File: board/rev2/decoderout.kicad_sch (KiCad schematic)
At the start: 12 parts, among them U10 IS61LV256AL, U11 74AHCT595

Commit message: Board GPIO allocation
- and usbmux

still need to do termination on the big buses + a bunch of bypass caps
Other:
- company: (none) -> MLABS
- title: (none) -> LED Bitstream Generator (gamma LUT + shifter)
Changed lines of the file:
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@@
 	(generator_version "9.0")
 	(paper "A4")
+	(title_block
+		(title "LED Bitstream Generator (gamma LUT + shifter)")
+		(rev "A")
+		(company "MLABS")
+		(comment 1 "MSign-NG")
+	)
 	(text "Gamma correction table (PIX_MEM)"
 		(exclude_from_sim no)

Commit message: Continue board, assign caps/res, adjust for JLC availability
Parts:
- C31, C32: footprint (none) -> Capacitor_SMD:C_0402_1005Metric; Part (none) -> CL05B104KB54PNC
- R13, R14, R15, R16, R17, R18, R19: footprint (none) -> Resistor_SMD:R_0402_1005Metric; Part (none) -> 0402WGF1001TCE
- R20: footprint (none) -> Resistor_SMD:R_0805_2012Metric; Part (none) -> 0805W8F1002T5E
- U11: footprint (none) -> Package_SO:TSSOP-16_4.4x5mm_P0.65mm
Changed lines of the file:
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@@
 			)
 		)
-		(property "Footprint" ""
+		(property "Footprint" "Capacitor_SMD:C_0402_1005Metric"
 			(at 114.3 73.66 0)
 			(effects
@@
 			)
 		)
+		(property "Part" "CL05B104KB54PNC"
+			(at 114.3 73.66 90)
+			(effects
+				(font
+					(size 1.27 1.27)
+				)
+				(hide yes)
+			)
+		)
 		(pin "2"
 		)
@@
 			)
 		)
-		(property "Footprint" ""
+		(property "Footprint" "Resistor_SMD:R_0402_1005Metric"
 			(at 139.7 102.87 0)
 			(effects
@@
 			)
 		)
+		(property "Part" "0402WGF1001TCE"
+			(at 139.7 102.87 90)
+			(effects
+				(font
+					(size 1.27 1.27)
+				)
+				(hide yes)
+			)
+		)
 		(pin "2"
 		)
@@
 			)
 		)
-		(property "Footprint" ""
+		(property "Footprint" "Resistor_SMD:R_0402_1005Metric"
 			(at 139.7 95.25 0)
 			(effects
@@
 			)
 		)
+		(property "Part" "0402WGF1001TCE"
+			(at 139.7 95.25 90)
+			(effects
+				(font
+					(size 1.27 1.27)
+				)
+				(hide yes)
+			)
+		)
 		(pin "2"
 		)
@@
 			)
 		)
-		(property "Footprint" ""
+		(property "Footprint" "Resistor_SMD:R_0402_1005Metric"
 			(at 139.7 105.41 0)
 			(effects
@@
 					(size 1.27 1.27)
 					(color 255 255 194 1)
+				)
+				(hide yes)
+			)
+		)
+		(property "Part" "0402WGF1001TCE"
+			(at 139.7 105.41 90)
+			(effects
+				(font
+					(size 1.27 1.27)
 				)
 				(hide yes)
@@
 			)
 		)
-		(property "Footprint" ""
+		(property "Footprint" "Package_SO:TSSOP-16_4.4x5mm_P0.65mm"
 			(at 184.15 97.79 0)
 			(effects
@@
 			)
 		)
-		(property "Footprint" ""
+		(property "Footprint" "Resistor_SMD:R_0402_1005Metric"
 			(at 139.7 100.33 0)
 			(effects
@@
 			)
 		)
+		(property "Part" "0402WGF1001TCE"
+			(at 139.7 100.33 90)
+			(effects
+				(font
+					(size 1.27 1.27)
+				)
+				(hide yes)
+			)
+		)
 		(pin "2"
 		)
@@
 			)
 		)
-		(property "Footprint" ""
+		(property "Footprint" "Resistor_SMD:R_0402_1005Metric"
 			(at 139.7 92.71 0)
 			(effects
@@
 			)
 		)
+		(property "Part" "0402WGF1001TCE"
+			(at 139.7 92.71 90)
+			(effects
+				(font
+					(size 1.27 1.27)
+				)
+				(hide yes)
+			)
+		)
 		(pin "2"
 		)
@@
 			)
 		)
-		(property "Footprint" ""
+		(property "Footprint" "Resistor_SMD:R_0402_1005Metric"
 			(at 139.7 97.79 0)
 			(effects
@@
 					(size 1.27 1.27)
 					(color 255 255 194 1)
+				)
+				(hide yes)
+			)
+		)
+		(property "Part" "0402WGF1001TCE"
+			(at 139.7 97.79 90)
+			(effects
+				(font
+					(size 1.27 1.27)
 				)
 				(hide yes)
@@
 			)
 		)
-		(property "Footprint" ""
+		(property "Footprint" "Capacitor_SMD:C_0402_1005Metric"
 			(at 191.77 76.2 0)
 			(effects
@@
 			)
 		)
+		(property "Part" "CL05B104KB54PNC"
+			(at 191.77 76.2 90)
+			(effects
+				(font
+					(size 1.27 1.27)
+				)
+				(hide yes)
+			)
+		)
 		(pin "2"
 		)
@@
 			)
 		)
-		(property "Footprint" ""
+		(property "Footprint" "Resistor_SMD:R_0402_1005Metric"
 			(at 139.7 90.17 0)
 			(effects
@@
 					(size 1.27 1.27)
 					(color 255 255 194 1)
+				)
+				(hide yes)
+			)
+		)
+		(property "Part" "0402WGF1001TCE"
+			(at 139.7 90.17 90)
+			(effects
+				(font
+					(size 1.27 1.27)
 				)
 				(hide yes)
@@
 			)
 		)
-		(property "Footprint" ""
+		(property "Footprint" "Resistor_SMD:R_0805_2012Metric"
 			(at 165.1 83.82 0)
 			(effects
@@
 				)
 				(hide yes)
+			)
+		)
+		(property "Part" "0805W8F1002T5E"
+			(at 165.1 83.82 0)
+			(effects
+				(font
+					(size 1.27 1.27)
+				)
+				(hide yes)

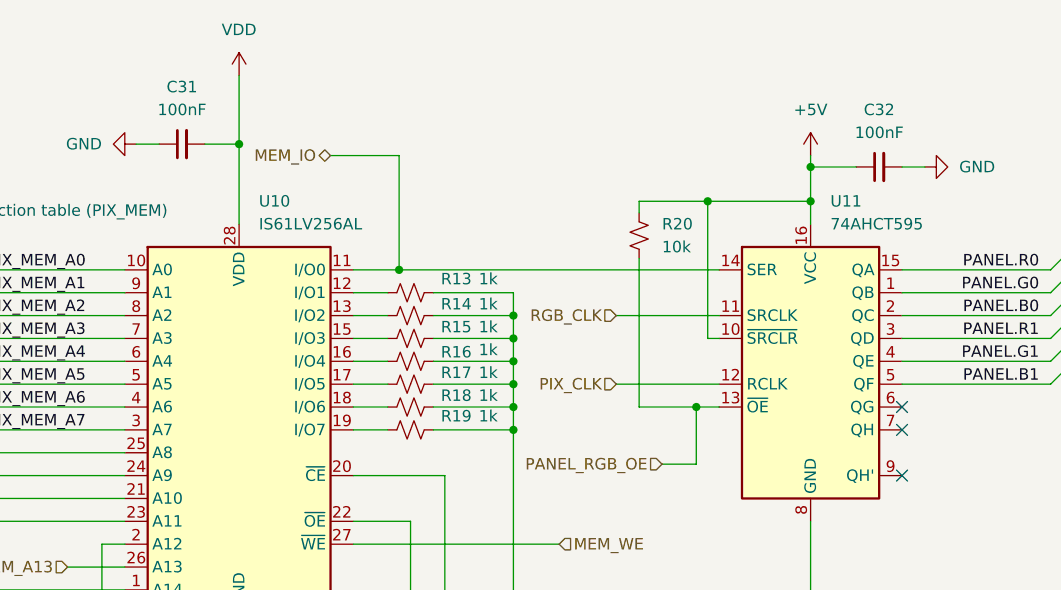
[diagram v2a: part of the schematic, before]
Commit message: Start new PCB
- all footprints setup
- need to setup netclasses next, tho
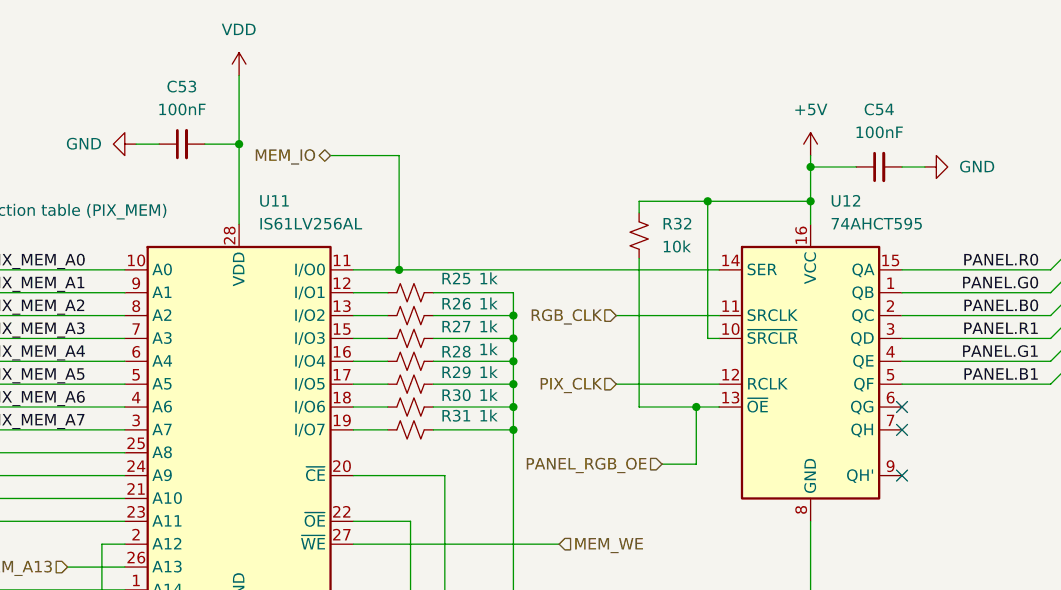
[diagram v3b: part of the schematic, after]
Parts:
- U11: renamed from U10; footprint Package_SO:SOP-28_8.4x18.16mm_P1.27mm -> Package_TSOPI:TSOP-28_L11.8-W8.0-P0.55-LS13.4-L; Part (none) -> IS61LV256AL
- U12: renamed from U11; Part (none) -> 74AHCT595
- renumbered C31 to C53, C32 to C54, R13 to R25, R14 to R26, R15 to R27, R16 to R28, R17 to R29, R18 to R30, R19 to R31, R20 to R32

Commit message: Really finish rev2 board schematic
- fix some more footprints
  - move to real SD card holder, for example
- repair part numbers
- add LCSC part refs to everything
- add even more caps to the 3.3V reg output
  - really should use an LDO but meh it should be fine

total BOM cost for 5 of them is apparently 160 CAD, or like 32 dollars
each (don't think that includes the feeder fees tho)
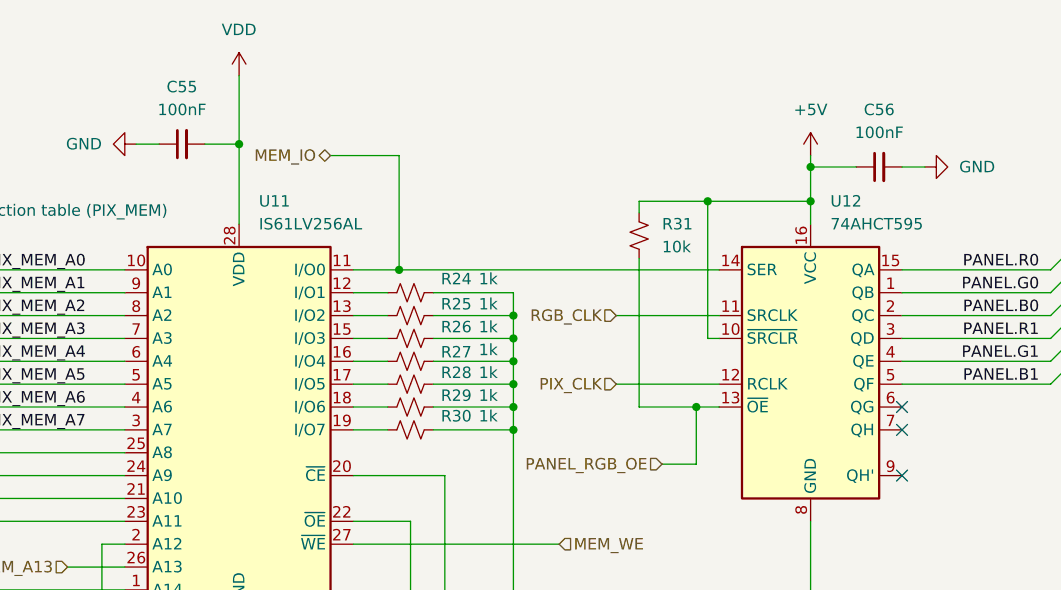
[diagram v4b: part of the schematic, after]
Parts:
- C55: renamed from C53; LCSC (none) -> C307331
- C56: renamed from C54; LCSC (none) -> C307331
- R24: renamed from R25; LCSC (none) -> C11702
- R25: renamed from R26; LCSC (none) -> C11702
- R26: renamed from R27; LCSC (none) -> C11702
- R27: renamed from R28; LCSC (none) -> C11702
- R28: renamed from R29; LCSC (none) -> C11702
- R29: renamed from R30; LCSC (none) -> C11702
- R30: renamed from R31; LCSC (none) -> C11702
- R31: renamed from R32; LCSC (none) -> C17414
- U11: LCSC (none) -> C412837; Part IS61LV256AL -> IS61LV256AL-10TLI
- U12: LCSC (none) -> C460504; Part 74AHCT595 -> 74AHCT595T16-13

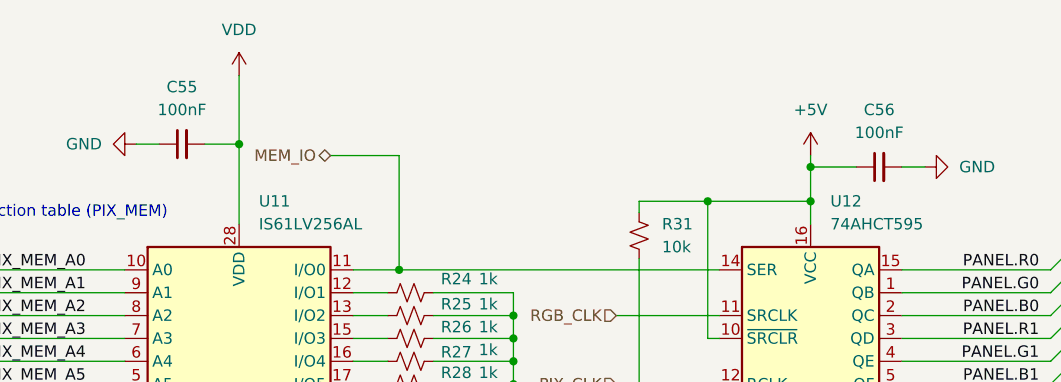
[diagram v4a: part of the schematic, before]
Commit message: Start board
add a few extra bypass caps too, and swap some pins on the USB mux

i forgot to add a bypass cap on the tpd6s so that also needs to happen

truly 63 capacitors is not enough
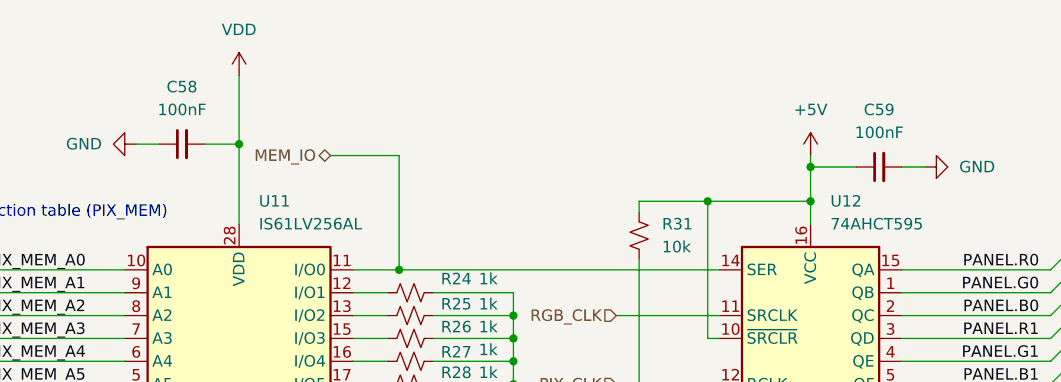
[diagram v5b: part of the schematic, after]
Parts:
- renumbered C55 to C58, C56 to C59
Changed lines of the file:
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@@
 		(dnp no)
 		(fields_autoplaced yes)
-		(property "Reference" "C55"
+		(property "Reference" "C58"
 			(at 114.3063 67.31 90)
 			(effects
@@
 			(project "mainboard"
 				(path "/32eb05c7-b4a6-42f3-8fb3-43453631100f/2c9586de-ca2f-4a0b-8ff8-8fdad1d1abcc/1fdb9a92-7450-4af0-9e02-ab97d3a0a007"
-					(reference "C55")
-					(unit 1)
-				)
-				(path "/32eb05c7-b4a6-42f3-8fb3-43453631100f/2c9586de-ca2f-4a0b-8ff8-8fdad1d1abcc/3c07b397-7ce8-476f-8583-4e671a583d8a"
-					(reference "C57")
+					(reference "C58")
+					(unit 1)
+				)
+				(path "/32eb05c7-b4a6-42f3-8fb3-43453631100f/2c9586de-ca2f-4a0b-8ff8-8fdad1d1abcc/3c07b397-7ce8-476f-8583-4e671a583d8a"
+					(reference "C60")
 					(unit 1)
 				)
@@
 		(dnp no)
 		(fields_autoplaced yes)
-		(property "Reference" "#PWR039"
+		(property "Reference" "#PWR040"
 			(at 184.15 78.74 0)
 			(effects
@@
 			(project "mainboard"
 				(path "/32eb05c7-b4a6-42f3-8fb3-43453631100f/2c9586de-ca2f-4a0b-8ff8-8fdad1d1abcc/1fdb9a92-7450-4af0-9e02-ab97d3a0a007"
-					(reference "#PWR039")
-					(unit 1)
-				)
-				(path "/32eb05c7-b4a6-42f3-8fb3-43453631100f/2c9586de-ca2f-4a0b-8ff8-8fdad1d1abcc/3c07b397-7ce8-476f-8583-4e671a583d8a"
-					(reference "#PWR044")
+					(reference "#PWR040")
+					(unit 1)
+				)
+				(path "/32eb05c7-b4a6-42f3-8fb3-43453631100f/2c9586de-ca2f-4a0b-8ff8-8fdad1d1abcc/3c07b397-7ce8-476f-8583-4e671a583d8a"
+					(reference "#PWR045")
 					(unit 1)
 				)
@@
 		(dnp no)
 		(fields_autoplaced yes)
-		(property "Reference" "#PWR036"
+		(property "Reference" "#PWR037"
 			(at 102.87 73.66 0)
 			(effects
@@
 			(project "mainboard"
 				(path "/32eb05c7-b4a6-42f3-8fb3-43453631100f/2c9586de-ca2f-4a0b-8ff8-8fdad1d1abcc/1fdb9a92-7450-4af0-9e02-ab97d3a0a007"
-					(reference "#PWR036")
-					(unit 1)
-				)
-				(path "/32eb05c7-b4a6-42f3-8fb3-43453631100f/2c9586de-ca2f-4a0b-8ff8-8fdad1d1abcc/3c07b397-7ce8-476f-8583-4e671a583d8a"
-					(reference "#PWR041")
+					(reference "#PWR037")
+					(unit 1)
+				)
+				(path "/32eb05c7-b4a6-42f3-8fb3-43453631100f/2c9586de-ca2f-4a0b-8ff8-8fdad1d1abcc/3c07b397-7ce8-476f-8583-4e671a583d8a"
+					(reference "#PWR042")
 					(unit 1)
 				)
@@
 		(on_board yes)
 		(dnp no)
-		(property "Reference" "#PWR040"
+		(property "Reference" "#PWR041"
 			(at 203.2 76.2 0)
 			(effects
@@
 			(project "mainboard"
 				(path "/32eb05c7-b4a6-42f3-8fb3-43453631100f/2c9586de-ca2f-4a0b-8ff8-8fdad1d1abcc/1fdb9a92-7450-4af0-9e02-ab97d3a0a007"
-					(reference "#PWR040")
-					(unit 1)
-				)
-				(path "/32eb05c7-b4a6-42f3-8fb3-43453631100f/2c9586de-ca2f-4a0b-8ff8-8fdad1d1abcc/3c07b397-7ce8-476f-8583-4e671a583d8a"
-					(reference "#PWR045")
+					(reference "#PWR041")
+					(unit 1)
+				)
+				(path "/32eb05c7-b4a6-42f3-8fb3-43453631100f/2c9586de-ca2f-4a0b-8ff8-8fdad1d1abcc/3c07b397-7ce8-476f-8583-4e671a583d8a"
+					(reference "#PWR046")
 					(unit 1)
 				)
@@
 		(dnp no)
 		(fields_autoplaced yes)
-		(property "Reference" "#PWR038"
+		(property "Reference" "#PWR039"
 			(at 120.65 139.7 0)
 			(effects
@@
 			(project "mainboard"
 				(path "/32eb05c7-b4a6-42f3-8fb3-43453631100f/2c9586de-ca2f-4a0b-8ff8-8fdad1d1abcc/1fdb9a92-7450-4af0-9e02-ab97d3a0a007"
-					(reference "#PWR038")
-					(unit 1)
-				)
-				(path "/32eb05c7-b4a6-42f3-8fb3-43453631100f/2c9586de-ca2f-4a0b-8ff8-8fdad1d1abcc/3c07b397-7ce8-476f-8583-4e671a583d8a"
-					(reference "#PWR043")
+					(reference "#PWR039")
+					(unit 1)
+				)
+				(path "/32eb05c7-b4a6-42f3-8fb3-43453631100f/2c9586de-ca2f-4a0b-8ff8-8fdad1d1abcc/3c07b397-7ce8-476f-8583-4e671a583d8a"
+					(reference "#PWR044")
 					(unit 1)
 				)
@@
 		(dnp no)
 		(fields_autoplaced yes)
-		(property "Reference" "C56"
+		(property "Reference" "C59"
 			(at 191.7763 69.85 90)
 			(effects
@@
 			(project "mainboard"
 				(path "/32eb05c7-b4a6-42f3-8fb3-43453631100f/2c9586de-ca2f-4a0b-8ff8-8fdad1d1abcc/1fdb9a92-7450-4af0-9e02-ab97d3a0a007"
-					(reference "C56")
-					(unit 1)
-				)
-				(path "/32eb05c7-b4a6-42f3-8fb3-43453631100f/2c9586de-ca2f-4a0b-8ff8-8fdad1d1abcc/3c07b397-7ce8-476f-8583-4e671a583d8a"
-					(reference "C58")
+					(reference "C59")
+					(unit 1)
+				)
+				(path "/32eb05c7-b4a6-42f3-8fb3-43453631100f/2c9586de-ca2f-4a0b-8ff8-8fdad1d1abcc/3c07b397-7ce8-476f-8583-4e671a583d8a"
+					(reference "C61")
 					(unit 1)
 				)
@@
 		(dnp no)
 		(fields_autoplaced yes)
-		(property "Reference" "#PWR037"
+		(property "Reference" "#PWR038"
 			(at 120.65 69.85 0)
 			(effects
@@
 			(project "mainboard"
 				(path "/32eb05c7-b4a6-42f3-8fb3-43453631100f/2c9586de-ca2f-4a0b-8ff8-8fdad1d1abcc/1fdb9a92-7450-4af0-9e02-ab97d3a0a007"
-					(reference "#PWR037")
-					(unit 1)
-				)
-				(path "/32eb05c7-b4a6-42f3-8fb3-43453631100f/2c9586de-ca2f-4a0b-8ff8-8fdad1d1abcc/3c07b397-7ce8-476f-8583-4e671a583d8a"
-					(reference "#PWR042")
-					(unit 1)
-				)
+					(reference "#PWR038")
+					(unit 1)
+				)
+				(path "/32eb05c7-b4a6-42f3-8fb3-43453631100f/2c9586de-ca2f-4a0b-8ff8-8fdad1d1abcc/3c07b397-7ce8-476f-8583-4e671a583d8a"
+					(reference "#PWR043")
+					(unit 1)
+				)

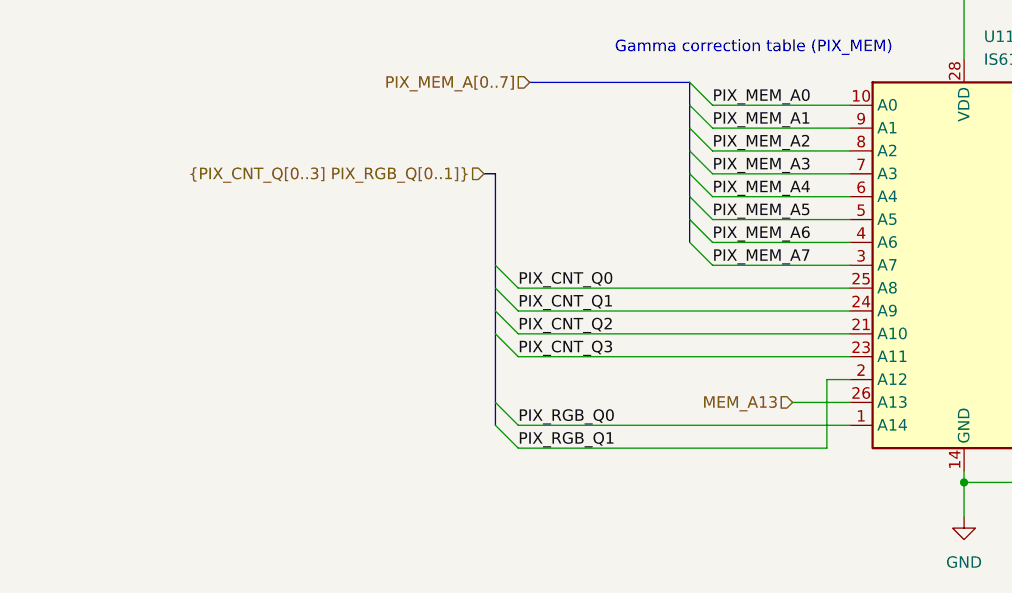
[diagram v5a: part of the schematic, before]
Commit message: More tweaks to schematic, start laying out regulators
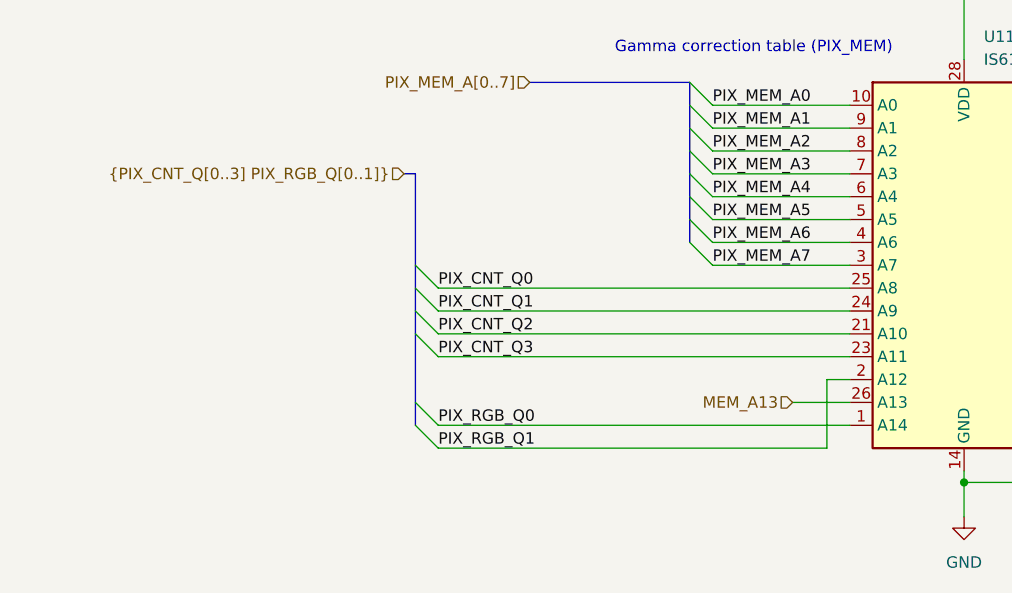
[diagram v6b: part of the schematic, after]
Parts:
- R31: footprint Resistor_SMD:R_0805_2012Metric -> Resistor_SMD:R_0402_1005Metric; LCSC C17414 -> C25744; Part 0805W8F1002T5E -> 0402WGF1002TCE
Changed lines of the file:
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@@
 	)
 	(bus_entry
-		(at 68.58 113.03)
+		(at 59.69 113.03)
 		(size 2.54 2.54)
 		(stroke
@@
 	)
 	(bus_entry
-		(at 68.58 123.19)
+		(at 59.69 123.19)
 		(size 2.54 2.54)
 		(stroke
@@
 	)
 	(bus_entry
-		(at 68.58 120.65)
+		(at 59.69 120.65)
 		(size 2.54 2.54)
 		(stroke
@@
 	)
 	(bus_entry
-		(at 68.58 107.95)
+		(at 59.69 107.95)
 		(size 2.54 2.54)
 		(stroke
@@
 	)
 	(bus_entry
-		(at 68.58 105.41)
+		(at 59.69 105.41)
 		(size 2.54 2.54)
 		(stroke
@@
 	)
 	(bus_entry
-		(at 68.58 110.49)
+		(at 59.69 110.49)
 		(size 2.54 2.54)
 		(stroke
@@
 	(wire
 		(pts
-			(xy 71.12 113.03) (xy 107.95 113.03)
+			(xy 62.23 113.03) (xy 107.95 113.03)
 		)
 		(stroke
@@
 	(wire
 		(pts
-			(xy 71.12 107.95) (xy 107.95 107.95)
+			(xy 62.23 107.95) (xy 107.95 107.95)
 		)
 		(stroke
@@
 	(wire
 		(pts
-			(xy 71.12 110.49) (xy 107.95 110.49)
+			(xy 62.23 110.49) (xy 107.95 110.49)
 		)
 		(stroke
@@
 	(bus
 		(pts
-			(xy 68.58 107.95) (xy 68.58 110.49)
+			(xy 59.69 107.95) (xy 59.69 110.49)
 		)
 		(stroke
@@
 	(wire
 		(pts
-			(xy 71.12 115.57) (xy 107.95 115.57)
+			(xy 62.23 115.57) (xy 107.95 115.57)
 		)
 		(stroke
@@
 	(bus
 		(pts
-			(xy 67.31 95.25) (xy 68.58 95.25)
+			(xy 58.42 95.25) (xy 59.69 95.25)
 		)
 		(stroke
@@
 	(wire
 		(pts
-			(xy 71.12 123.19) (xy 107.95 123.19)
+			(xy 62.23 123.19) (xy 107.95 123.19)
 		)
 		(stroke
@@
 	(bus
 		(pts
-			(xy 68.58 120.65) (xy 68.58 123.19)
+			(xy 59.69 120.65) (xy 59.69 123.19)
 		)
 		(stroke
@@
 	(bus
 		(pts
-			(xy 68.58 113.03) (xy 68.58 120.65)
+			(xy 59.69 113.03) (xy 59.69 120.65)
 		)
 		(stroke
@@
 	(bus
 		(pts
-			(xy 68.58 95.25) (xy 68.58 105.41)
+			(xy 59.69 95.25) (xy 59.69 105.41)
 		)
 		(stroke
@@
 	(wire
 		(pts
-			(xy 71.12 125.73) (xy 105.41 125.73)
+			(xy 62.23 125.73) (xy 105.41 125.73)
 		)
 		(stroke
@@
 	(bus
 		(pts
-			(xy 68.58 110.49) (xy 68.58 113.03)
+			(xy 59.69 110.49) (xy 59.69 113.03)
 		)
 		(stroke
@@
 	(bus
 		(pts
-			(xy 68.58 105.41) (xy 68.58 107.95)
+			(xy 59.69 105.41) (xy 59.69 107.95)
 		)
 		(stroke
@@
 	)
 	(label "PIX_RGB_Q0"
-		(at 71.12 123.19 0)
+		(at 62.23 123.19 0)
 		(effects
 			(font
@@
 	)
 	(label "PIX_CNT_Q1"
-		(at 71.12 110.49 0)
+		(at 62.23 110.49 0)
 		(effects
 			(font
@@
 	)
 	(label "PIX_CNT_Q0"
-		(at 71.12 107.95 0)
+		(at 62.23 107.95 0)
 		(effects
 			(font
@@
 	)
 	(label "PIX_RGB_Q1"
-		(at 71.12 125.73 0)
+		(at 62.23 125.73 0)
 		(effects
 			(font
@@
 	)
 	(label "PIX_CNT_Q2"
-		(at 71.12 113.03 0)
+		(at 62.23 113.03 0)
 		(effects
 			(font
@@
 	)
 	(label "PIX_CNT_Q3"
-		(at 71.12 115.57 0)
+		(at 62.23 115.57 0)
 		(effects
 			(font
@@
 	(hierarchical_label "{PIX_CNT_Q[0..3] PIX_RGB_Q[0..1]}"
 		(shape input)
-		(at 67.31 95.25 180)
+		(at 58.42 95.25 180)
 		(effects
 			(font
@@
 			)
 		)
-		(property "Footprint" "Resistor_SMD:R_0805_2012Metric"
+		(property "Footprint" "Resistor_SMD:R_0402_1005Metric"
 			(at 165.1 83.82 0)
 			(effects
@@
 			)
 		)
-		(property "Part" "0805W8F1002T5E"
+		(property "Part" "0402WGF1002TCE"
 			(at 165.1 83.82 0)
 			(effects
@@
 			)
 		)
-		(property "LCSC" "C17414 "
+		(property "LCSC" "C25744"
 			(at 165.1 83.82 0)
 			(effects
